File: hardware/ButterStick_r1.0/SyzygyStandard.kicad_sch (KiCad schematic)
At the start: 19 parts, among them J4 SYZYGY-STD, U14 TLV62569DRL

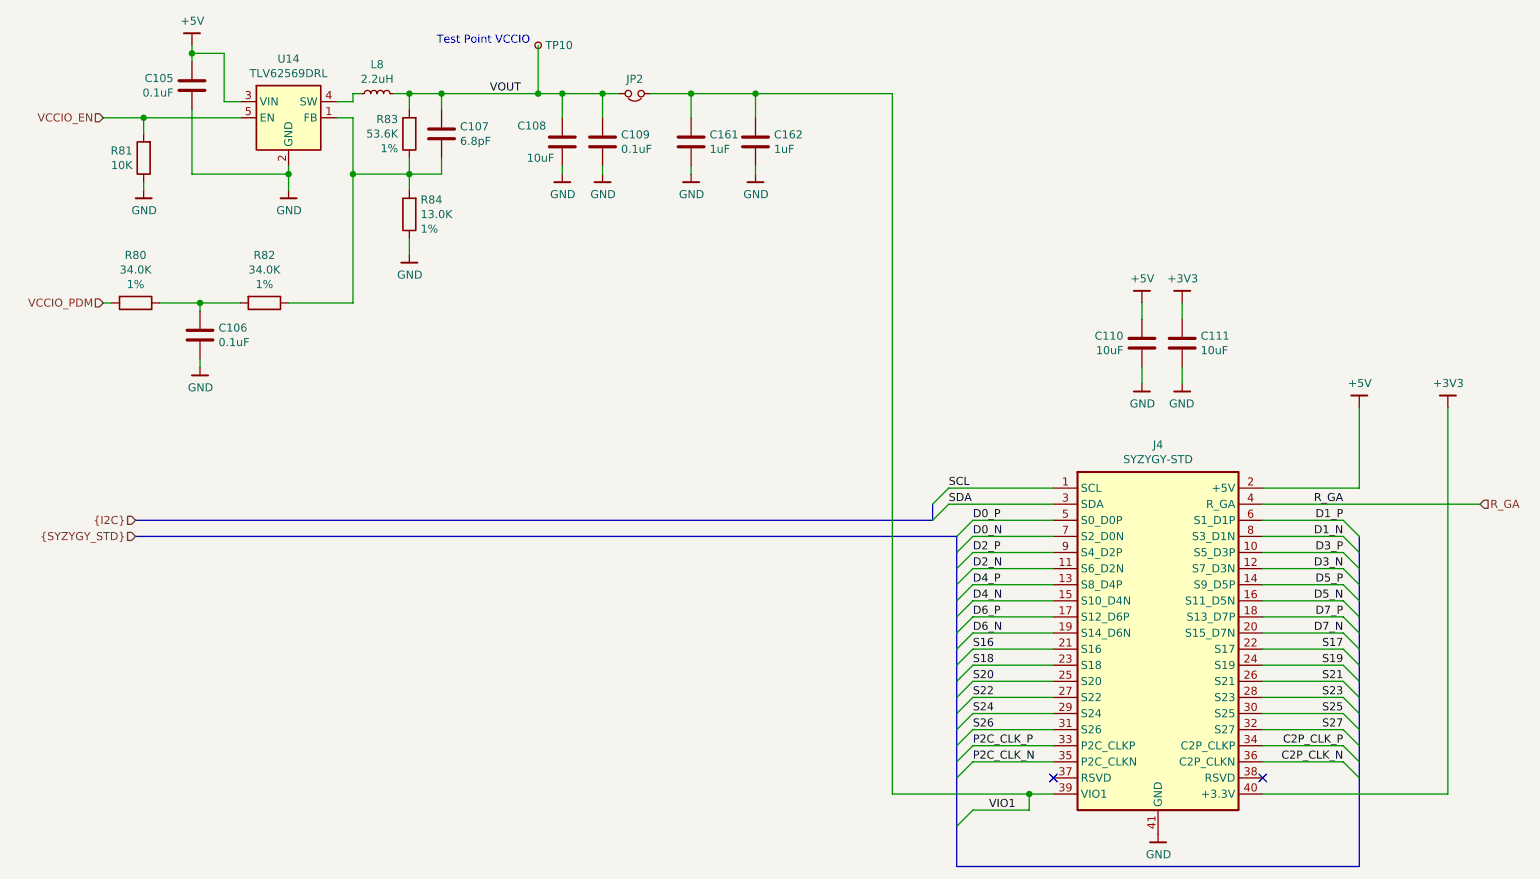
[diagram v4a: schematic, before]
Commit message: hardware.r1d0: Tidy up BOM entries
Export HTML Interactive BOM
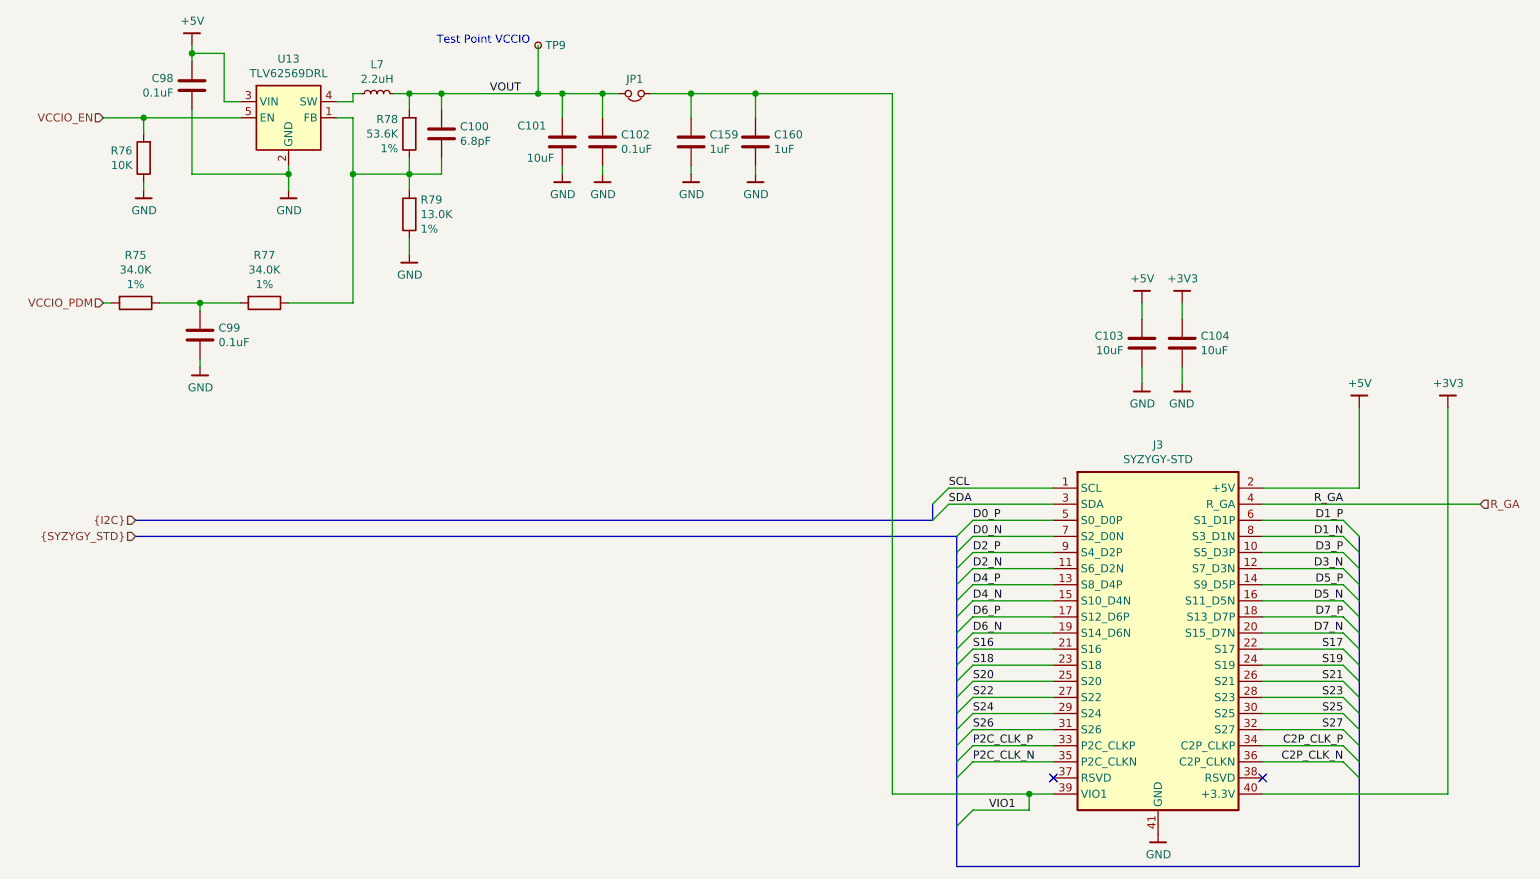
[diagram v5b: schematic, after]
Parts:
- JP1: renamed from JP2; now left out of the parts list
- renumbered C107 to C100, C108 to C101, C109 to C102, C110 to C103, C111 to C104, C161 to C159, C162 to C160, C105 to C98, C106 to C99, J4 to J3, L8 to L7, R80 to R75, R81 to R76, R82 to R77, R83 to R78, R84 to R79, TP10 to TP9, U14 to U13

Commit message: hardware.r1d0: Update USB0.reset pull
- Swap pulldown for pullup and re-route
- Regenerate gerbers, and schematic
- Update revision to r1.0a to reflect a hardware change
- Update silkscreen date

Fixes #8
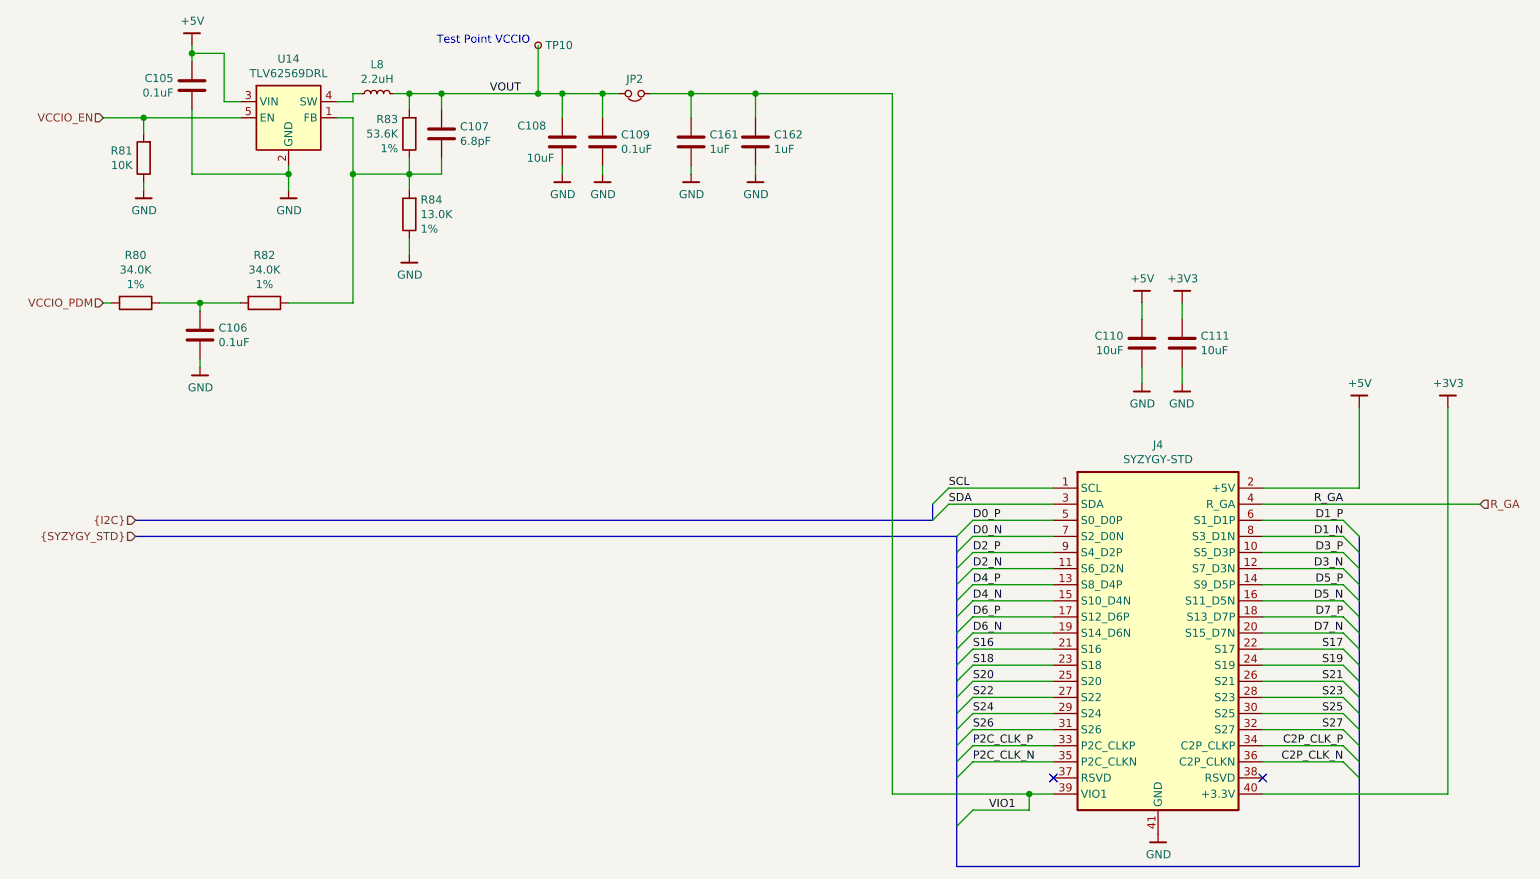
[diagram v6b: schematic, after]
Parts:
- renumbered C98 to C105, C99 to C106, C100 to C107, C101 to C108, C102 to C109, C103 to C110, C104 to C111, C159 to C161, C160 to C162, J3 to J4, JP1 to JP2, L7 to L8, R75 to R80, R76 to R81, R77 to R82, R78 to R83, R79 to R84, TP9 to TP10, U13 to U14

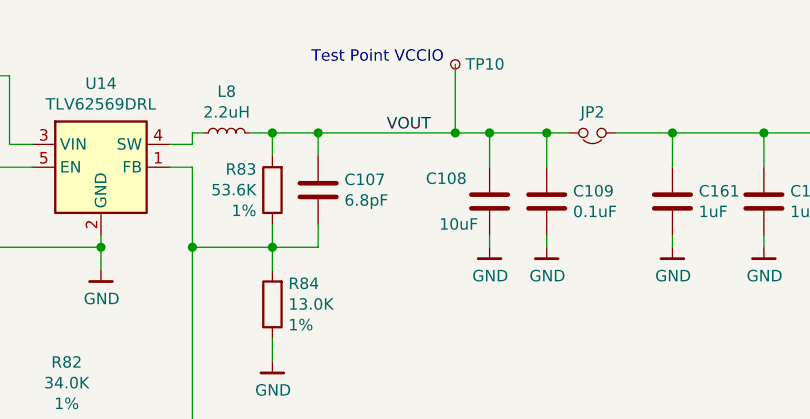
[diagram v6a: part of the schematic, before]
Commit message: Fix RGB G/B signals
- Corrects a mistake where blue and green signals were swapped
- Regenerate schematic

Closes #12
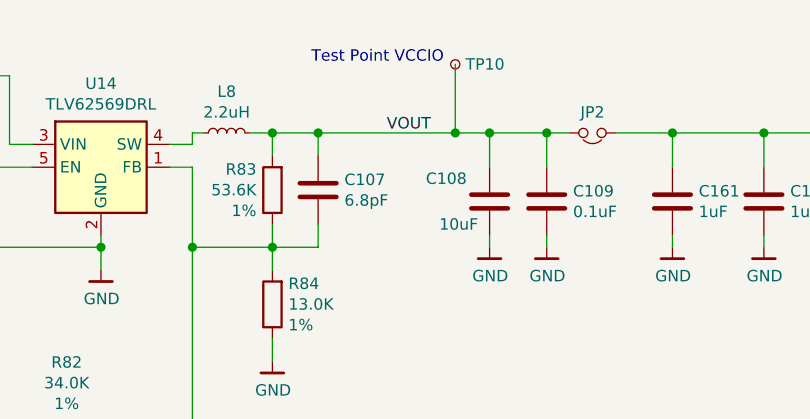
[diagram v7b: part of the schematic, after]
